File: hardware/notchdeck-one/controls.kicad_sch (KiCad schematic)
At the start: 38 parts, among them SW1 SW_Push, SW10 SW_Push, SW11 SW_Push, SW12 SW_Push, SW13 SW_Push, SW14 SW_Push, SW15 SW_Push, SW16 SW_Push, SW2 SW_Push, SW3 SW_Push, SW4 SW_Push, SW5 SW_Push, SW6 SW_Push, SW7 SW_Push, SW8 SW_Push, SW9 SW_Push

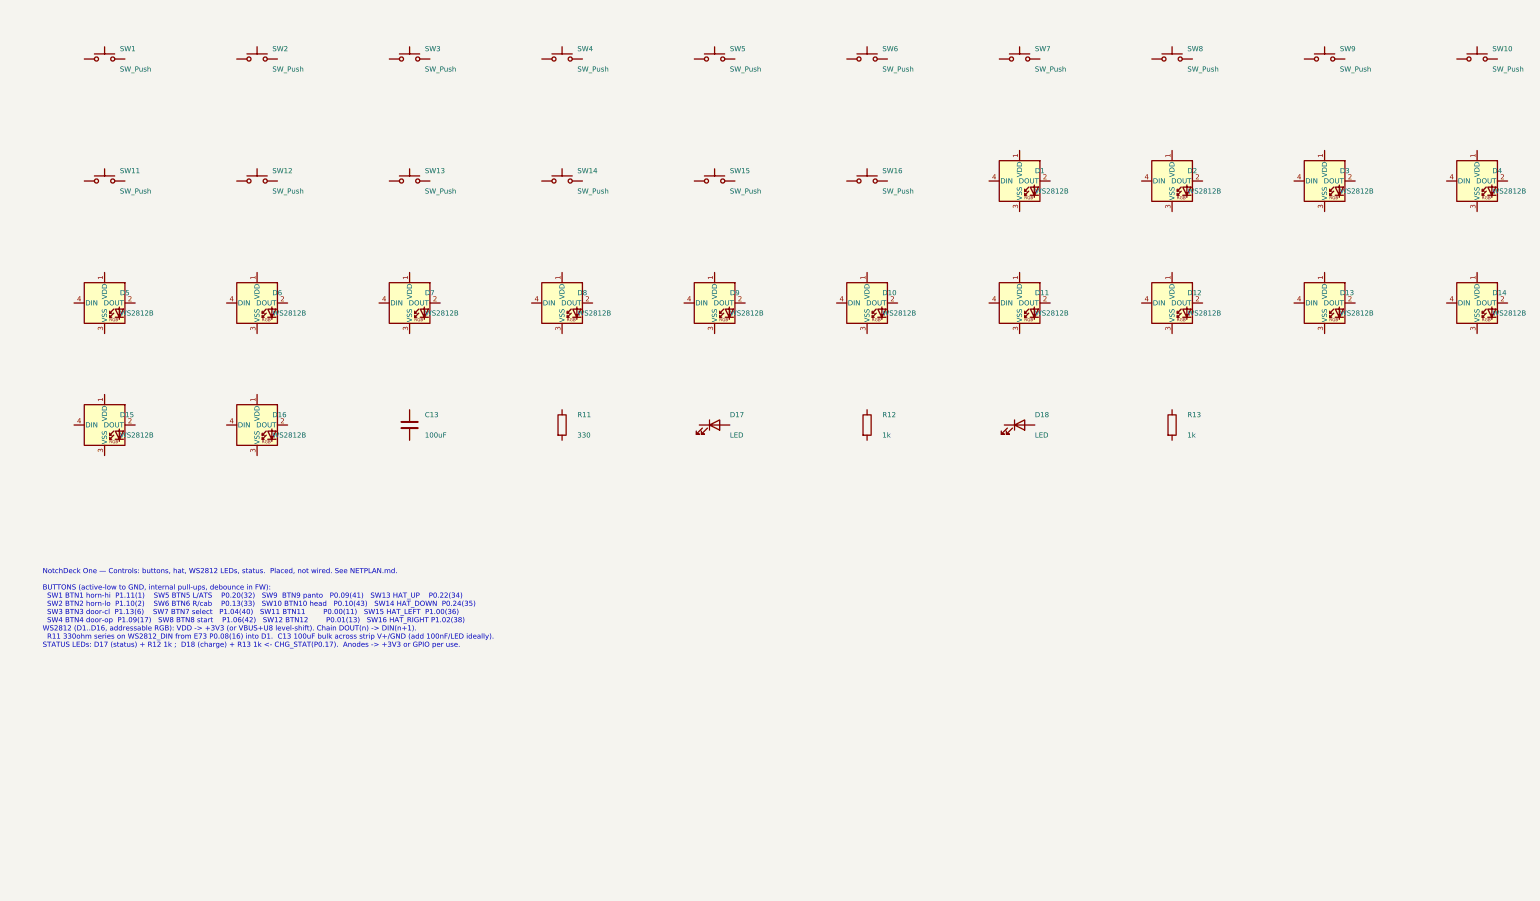
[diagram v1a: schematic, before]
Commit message: Wire and verify NotchDeck controller schematics
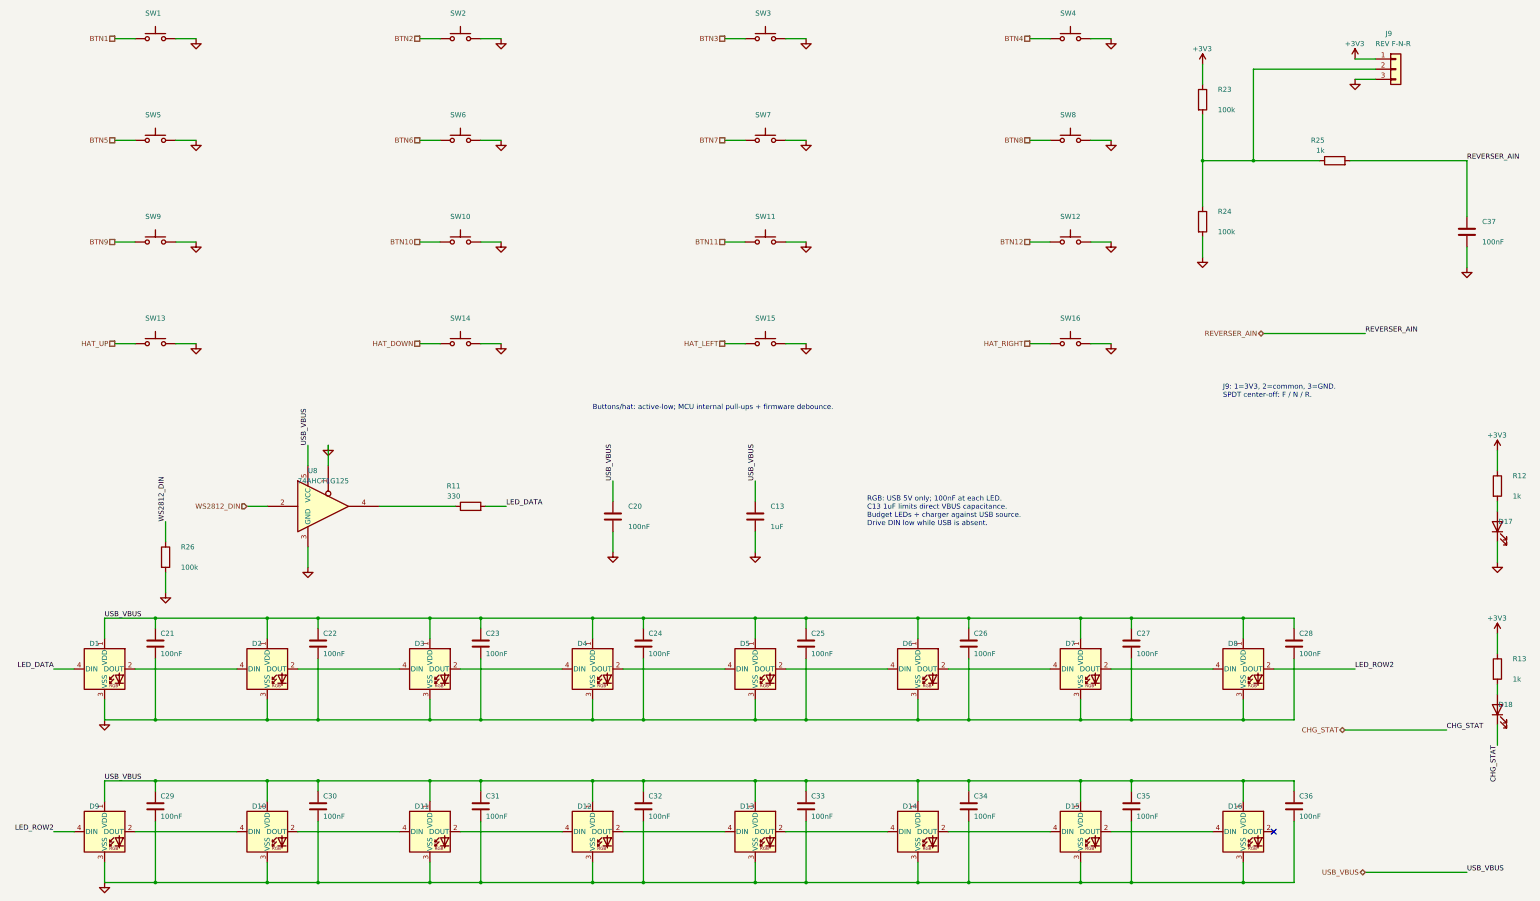
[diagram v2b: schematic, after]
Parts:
- added C20, C21, C22, C23, C24, C25, C26, C27, C28, C29, C30, C31, C32, C33, C34, C35, C36, C37: 100nF, Capacitor_SMD:C_0402_1005Metric, symbol Device:C
- added J9: REV F-N-R, Connector_JST:JST_PH_S3B-PH-SM4-TB_1x03-1MP_P2.00mm_Horizontal, symbol Connector_Generic:Conn_01x03
- added R23, R24, R26: 100k, Resistor_SMD:R_0402_1005Metric, symbol Device:R
- added R25: 1k, Resistor_SMD:R_0402_1005Metric, symbol Device:R
- added U8: 74AHCT1G125, Package_TO_SOT_SMD:SOT-23-5, symbol 74xGxx:74AHCT1G125
- C13: value 100uF -> 1uF; footprint Capacitor_SMD:C_1210_3225Metric -> Capacitor_SMD:C_0805_2012Metric
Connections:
- net HAT_LEFT: now reaches SW15.1
- net GND: now reaches SW15.2
- net GND: now also C13.2, D1.3 (VSS), D10.3 (VSS), D11.3 (VSS), D12.3 (VSS), D13.3 (VSS), D14.3 (VSS), D15.3 (VSS), D16.3 (VSS), D17.1 (K), D2.3 (VSS), D3.3 (VSS), D4.3 (VSS), D5.3 (VSS), D6.3 (VSS), D7.3 (VSS), D8.3 (VSS), D9.3 (VSS), SW1.2, SW10.2, SW11.2, SW12.2, SW13.2, SW14.2, SW16.2, SW2.2, SW3.2, SW4.2, SW5.2, SW6.2, SW7.2, SW8.2, SW9.2, C20.2, C21.2, C22.2, C23.2, C24.2, C25.2, C26.2, C27.2, C28.2, C29.2, C30.2, C31.2, C32.2, C33.2, C34.2, C35.2, C36.2, C37.2, J9.3 (Pin_3), R24.2, R26.2, U8.1, U8.3 (GND)
- net USB_VBUS: now reaches D7.1 (VDD)
- net USB_VBUS: now also C13.1, D1.1 (VDD), D10.1 (VDD), D11.1 (VDD), D12.1 (VDD), D13.1 (VDD), D14.1 (VDD), D15.1 (VDD), D16.1 (VDD), D2.1 (VDD), D3.1 (VDD), D4.1 (VDD), D5.1 (VDD), D6.1 (VDD), D8.1 (VDD), D9.1 (VDD), C20.1, C21.1, C22.1, C23.1, C24.1, C25.1, C26.1, C27.1, C28.1, C29.1, C30.1, C31.1, C32.1, C33.1, C34.1, C35.1, C36.1, U8.5 (VCC)
- net at D7.2 (DOUT): now also D8.4 (DIN)
- net at D7.4 (DIN): now also D6.2 (DOUT)
- net BTN7: now reaches SW7.1
- net HAT_RIGHT: now reaches SW16.1
- net at D2.2 (DOUT): now also D3.4 (DIN)
- net at D2.4 (DIN): now also D1.2 (DOUT)
- net BTN10: now reaches SW10.1
- net at D12.2 (DOUT): now also D13.4 (DIN)
- net at D12.4 (DIN): now also D11.2 (DOUT)
- net BTN2: now reaches SW2.1
- net at D4.2 (DOUT): now also D5.4 (DIN)
- net at D4.4 (DIN): now also D3.2 (DOUT)
- net at D5.2 (DOUT): now also D6.4 (DIN)
- net at D9.2 (DOUT): now also D10.4 (DIN)
- net LED_ROW2: now reaches D9.4 (DIN)
- net LED_ROW2: now also D8.2 (DOUT)
- net BTN6: now reaches SW6.1
- net +3V3: now reaches R12.1
- net +3V3: now also R13.1, J9.1 (Pin_1), R23.1
- net at R12.2: now also D17.2 (A)
- net BTN1: now reaches SW1.1
- net at D10.2 (DOUT): now also D11.4 (DIN)
- net LED_DATA: now reaches D1.4 (DIN)
- net LED_DATA: now also R11.2
- net BTN8: now reaches SW8.1
- net at D13.2 (DOUT): now also D14.4 (DIN)
- net BTN12: now reaches SW12.1
- net at R13.2: now also D18.2 (A)
- net at D15.2 (DOUT): now also D16.4 (DIN)
- net at D15.4 (DIN): now also D14.2 (DOUT)
- net CHG_STAT: now reaches D18.1 (K)
- net BTN9: now reaches SW9.1
- net HAT_DOWN: now reaches SW14.1
- net at R11.1: now also U8.4
- net BTN4: now reaches SW4.1
- net BTN11: now reaches SW11.1
- net BTN5: now reaches SW5.1
- net BTN3: now reaches SW3.1
- net HAT_UP: now reaches SW13.1
- new net: J9.2 (Pin_2), R23.2, R24.1, R25.1
- new net REVERSER_AIN: C37.1, R25.2
- new net WS2812_DIN: R26.1, U8.2
- no-connect marks 0 -> 1
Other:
- note added: "Buttons/hat: active-low; MCU internal pull-ups + firmware debounce."
- note added: "J9: 1=3V3, 2=common, 3=GND. SPDT center-off: F / N / R."
- note added: "RGB: USB 5V only; 100nF at each LED. C13 1uF limits direct VBUS capacitance. Budget LEDs + charger against USB source. Drive DIN low while USB is absent."
- note removed: "NotchDeck One — Controls: buttons, hat, WS2812 LEDs, status. Placed, not wired. See NETPLAN.md. BUTTONS (active-low to GND, internal pull-ups, debounce in FW): SW1 BTN1 horn-hi P1.11(1) SW5 BTN5 L/ATS P0.20(32) SW9 BTN9 panto P0.09(41) SW13 HAT_UP P0.22(34) SW2 BTN2 horn-lo P1.10(2) SW6 BTN6 R/cab P0.13(33) SW10 BTN10 head P0.10(43) SW14 HAT_DOWN P0.24(35) SW3 BTN3 door-cl P1.13(6) SW7 BTN7 selec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"
- title: NotchDeck One — Controls (buttons / hat / WS2812 LEDs / status) -> NotchDeck One — Controls and indicators

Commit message: Source controller BOM from JLCPCB and align selected footprints
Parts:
- C13: BOM Checked (none) -> 2026-10-03; BOM Comments (none) -> 1uF 50V X7R ±10% 0805 Multilayer Ceramic Capacitors MLCC - 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; JLCPCB Part Type (none) -> Basic; LCSC (none) -> C28323; MPN (none) -> CL21B105KBFNNNE; Manufacturer (none) -> Samsung Electro-Mechanics
- C20, C21, C22, C23, C24, C25, C26, C27, C28, C29, C30, C31, C32, C33, C34, C35, C36, C37: BOM Checked (none) -> 2026-10-03; BOM Comments (none) -> 100nF 16V X7R ±10% 0402 Multilayer Ceramic Capacitors MLCC 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; JLCPCB Part Type (none) -> Basic; LCSC (none) -> C1525; MPN (none) -> CL05B104KO5NNNC; Manufacturer (none) -> Samsung Electro-Mechanics
- D1, D10, D11, D12, D13, D14, D15, D16, D2, D3, D4, D5, D6, D7, D8, D9: footprint LED_SMD:LED_OPSCO_SK6812_PLCC4_5.0x5.0mm_P3.1mm -> notchdeck:LED_XINGLIGHT_XL-5050RGBC-2812B; BOM Checked (none) -> 2026-10-03; BOM Comments (none) -> Same RGB part for D1-D16. Check pin 1 and polarity in CPL p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; JLCPCB Part Type (none) -> Extended; Manufacturer (none) -> XINGLIGHT
- D17: BOM Checked (none) -> 2026-10-03; JLCPCB Part Type (none) -> Extended; LCSC (none) -> C965805; MPN (none) -> XL-1608SYGC-06; Manufacturer (none) -> XINGLIGHT
- D18: BOM Checked (none) -> 2026-10-03; JLCPCB Part Type (none) -> Basic; LCSC (none) -> C2286; MPN (none) -> KT-0603R; Manufacturer (none) -> Hubei KENTO Elec
- J9: BOM Checked (none) -> 2026-10-03; BOM Comments (none) -> External center-off reverser and mating harness not include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; JLCPCB Part Type (none) -> Extended; LCSC (none) -> C265101; MPN S3B-PH-SM4-TB -> S3B-PH-SM4-TB(LF)(SN)
- R11: BOM Checked (none) -> 2026-10-03; BOM Comments (none) -> -55℃~+155℃ 330Ω 50V 62.5mW Thick Film Resistor ±1% ±100ppm/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; JLCPCB Part Type (none) -> Basic; LCSC (none) -> C25104; MPN (none) -> 0402WGF3300TCE; Manufacturer (none) -> UNI-ROYAL
- R12, R13, R25: BOM Checked (none) -> 2026-10-03; BOM Comments (none) -> -55℃~+155℃ 1kΩ 50V 62.5mW Thick Film Resistor ±1% ±100ppm/℃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; JLCPCB Part Type (none) -> Basic; LCSC (none) -> C11702; MPN (none) -> 0402WGF1001TCE; Manufacturer (none) -> UNI-ROYAL
- R23, R24, R26: BOM Checked (none) -> 2026-10-03; BOM Comments (none) -> -55℃~+155℃ 100kΩ 50V 62.5mW Thick Film Resistor ±1% ±100ppm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; JLCPCB Part Type (none) -> Basic; LCSC (none) -> C25741; MPN (none) -> 0402WGF1003TCE; Manufacturer (none) -> UNI-ROYAL
- SW1, SW10, SW11, SW12, SW13, SW14, SW15, SW16, SW2, SW3, SW4, SW5, SW6, SW7, SW8, SW9: BOM Checked (none) -> 2026-10-03; JLCPCB Part Type (none) -> Basic; LCSC (none) -> C318884; MPN (none) -> TS-1187A-B-A-B; Manufacturer (none) -> XKB Connection
- U8: BOM Checked (none) -> 2026-10-03; BOM Comments (none) -> AHCT with TTL-compatible input at 5 V required; do not subs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; JLCPCB Part Type (none) -> Extended; LCSC (none) -> C7484; Manufacturer Texas Instruments -> TI
